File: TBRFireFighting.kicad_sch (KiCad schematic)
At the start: 22 parts, among them J1 USB_C_Receptacle, Q1 BC817, Q2 BC817, U1 AMS1117-3.3, U2 CH340G, U3 ESP32-WROOM-32UE, U4 TP4056, Y1 12 Mhz

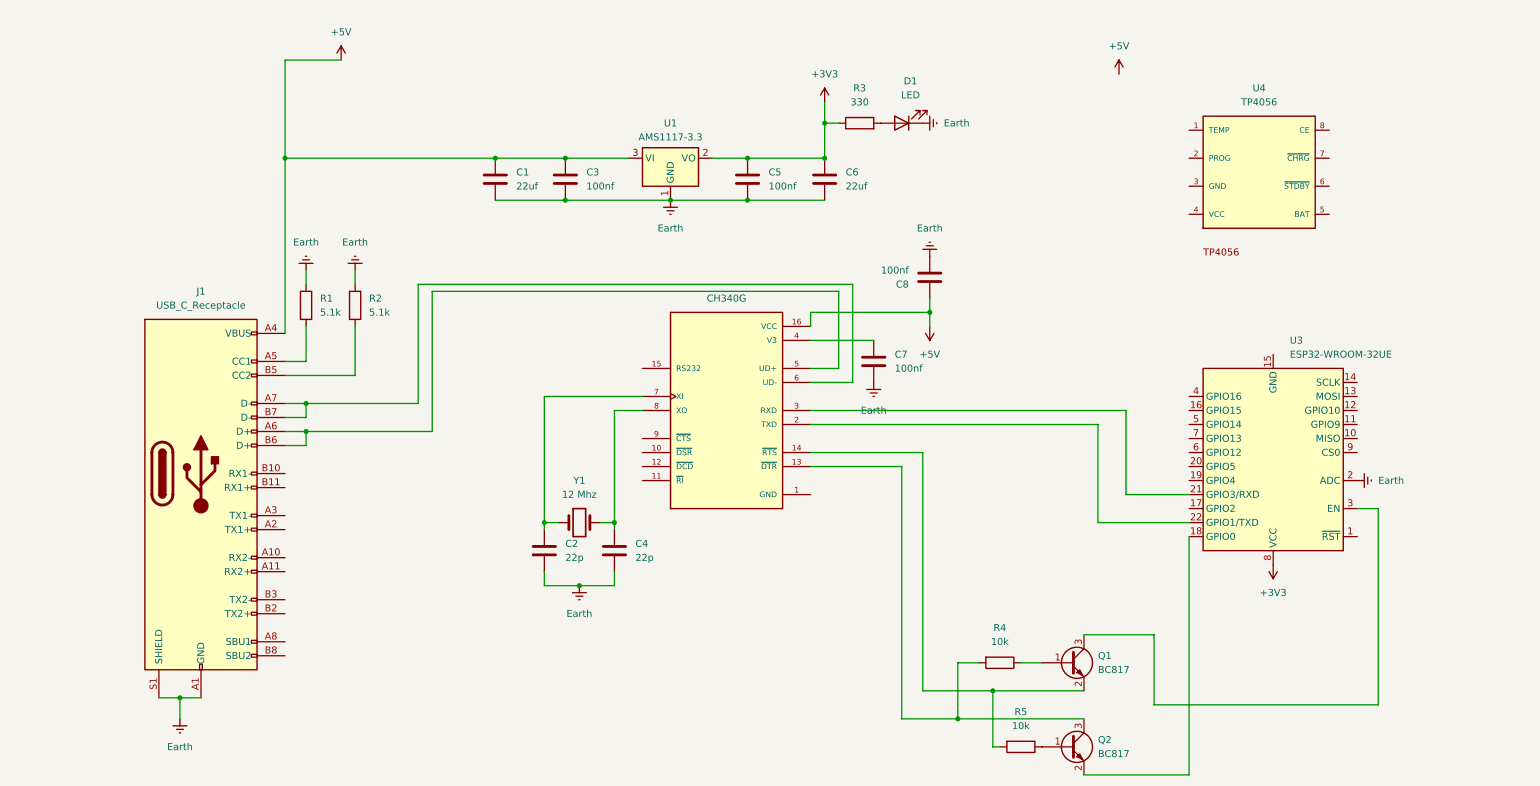
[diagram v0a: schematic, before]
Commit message: New esp32 Wrover E/IE
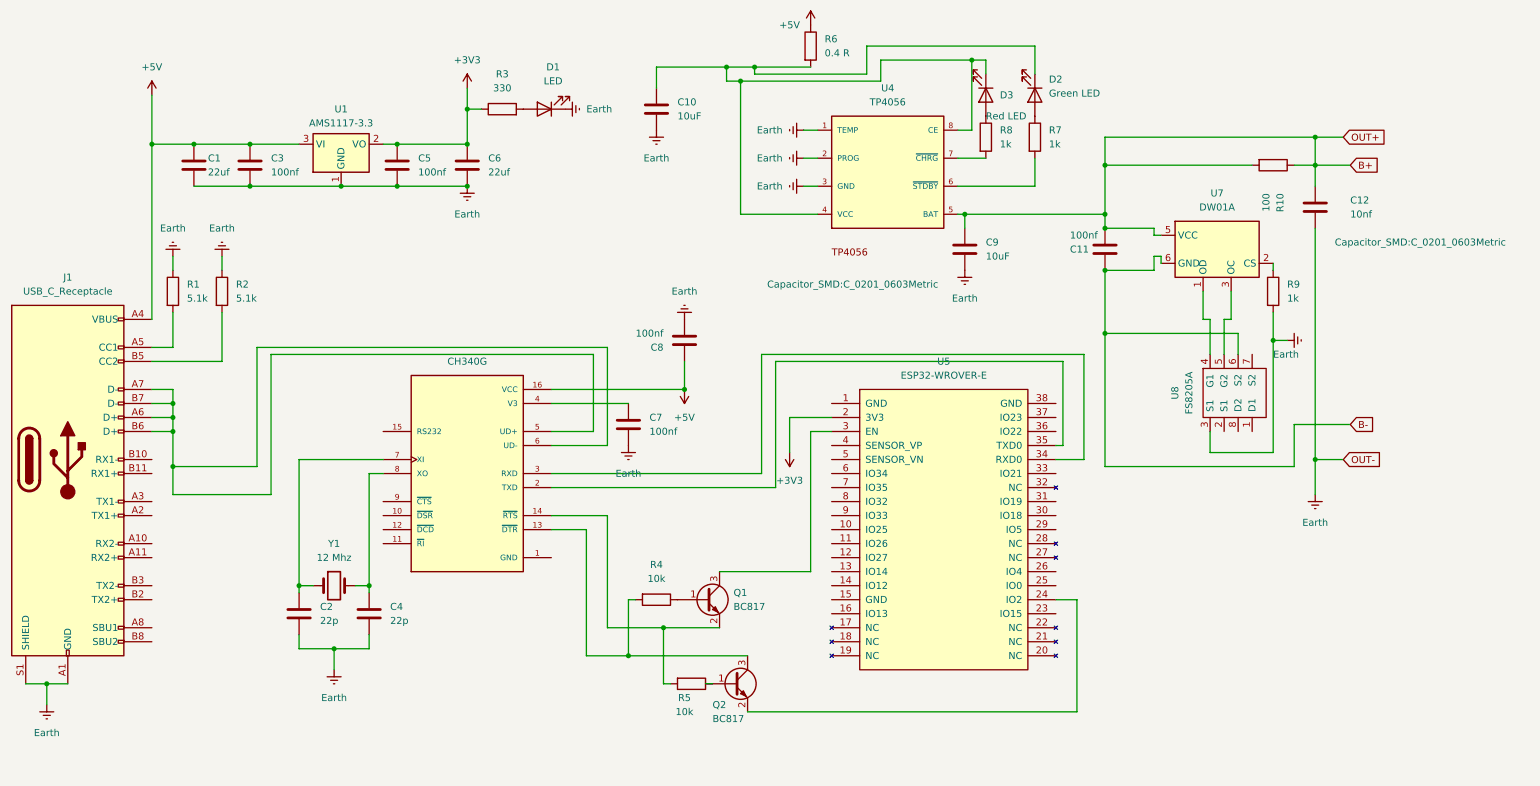
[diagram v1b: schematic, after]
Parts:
- removed U3: ESP32-WROOM-32UE, RF_Module:ESP-12E, symbol RF_Module:ESP-12F
- added C10: 10uF, symbol Device:C
- added C11: 100nf, Capacitor_SMD:C_0201_0603Metric, symbol Device:C
- added C12: 10nf, Capacitor_SMD:C_0201_0603Metric, symbol Device:C
- added C9: 10uF, Capacitor_SMD:C_0201_0603Metric, symbol Device:C
- added D2: Green LED, symbol Device:LED
- added D3: Red LED, symbol Device:LED
- added R10: 100, Resistor_SMD:R_1206_3216Metric, symbol Device:R
- added R6: 0.4 R, Resistor_SMD:R_1206_3216Metric, symbol Device:R
- added R7, R8, R9: 1k, Resistor_SMD:R_1206_3216Metric, symbol Device:R
- added U5: ESP32-WROVER-E, symbol EspressIf:ESP32-WROVER-E
- added U7: DW01A, Package_TO_SOT_SMD:SOT-23-6, symbol Battery_Management:DW01A
- added U8: FS8205A, Package_SO:TSSOP-8_4.4x3mm_P0.65mm, symbol fs8205a:FS8205A
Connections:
- net +3V3: now also U5.2 (3V3)
- net +5V: now also R6.1
- net Earth: now also U4.1 (TEMP), U4.2 (PROG), U4.3 (GND), C10.2, C12.2, C9.2, R9.2, U8.3 (S1)
- net at Q2.2 (E): now also U5.24 (IO2)
- net at U2.3 (RXD): now also U5.34 (RXD0)
- net at U2.2 (TXD): now also U5.35 (TXD0)
- net at Q1.3 (C): now also U5.3 (EN)
- net at J1.A6 (D+), J1.B6 (D+), U2.5 (UD+): now also J1.A7 (D-), J1.B7 (D-), U2.6 (UD-)
- net at U4.4 (VCC): now also U4.8 (CE), C10.1, D2.1 (K), D3.1 (K), R6.2
- net B+: now reaches U4.5 (BAT)
- net B+: now also C11.1, C12.1, C9.1, R10.1, R10.2, U7.5 (VCC)
- net at U4.6 (~{STDBY}): now also R7.2
- net at U4.7 (~{CHRG}): now also R8.2
- new net: D3.2 (A), R8.1
- new net: D2.2 (A), R7.1
- new net: U7.1 (OD), U8.4 (G1)
- new net: U7.3 (OC), U8.5 (G2)
- new net: R9.1, U7.2 (CS)
- new net B-: C11.2, U7.6 (GND), U8.6 (S2)
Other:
- moved on the sheet: C1, C2, C3, C4, C5, C6, C7, C8, D1, J1, Q1, Q2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
